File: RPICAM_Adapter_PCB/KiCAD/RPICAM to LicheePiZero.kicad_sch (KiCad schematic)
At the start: 6 parts, among them J1 RPI Camera Pin Out, U8 Lichee Pi Zero Headers

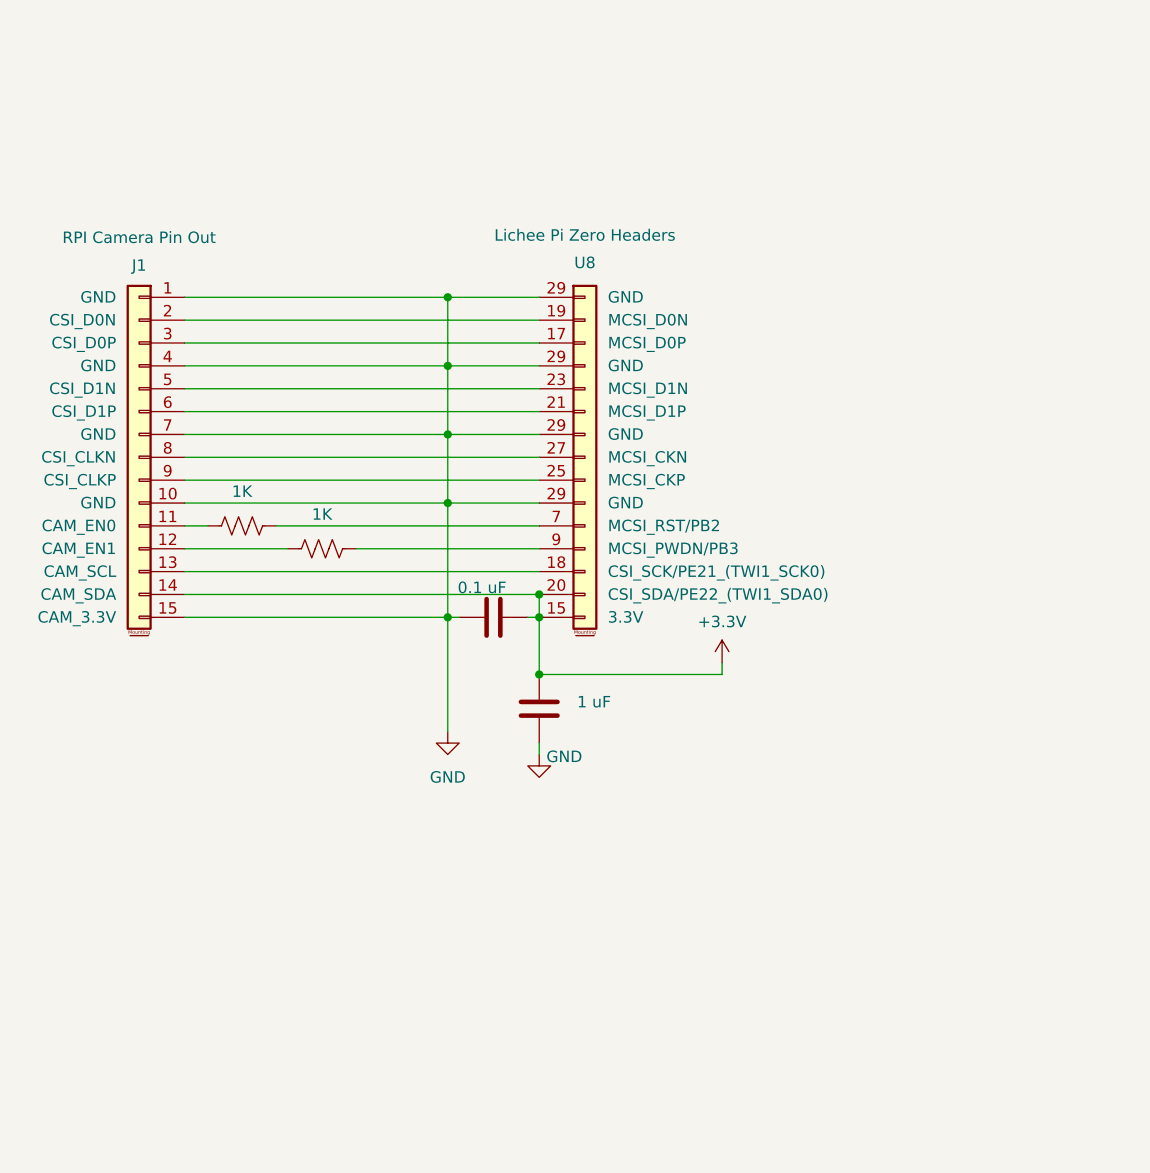
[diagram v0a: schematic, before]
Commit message: Changed I2C interface for MIPI_CSI adapter board to use CSI TWI
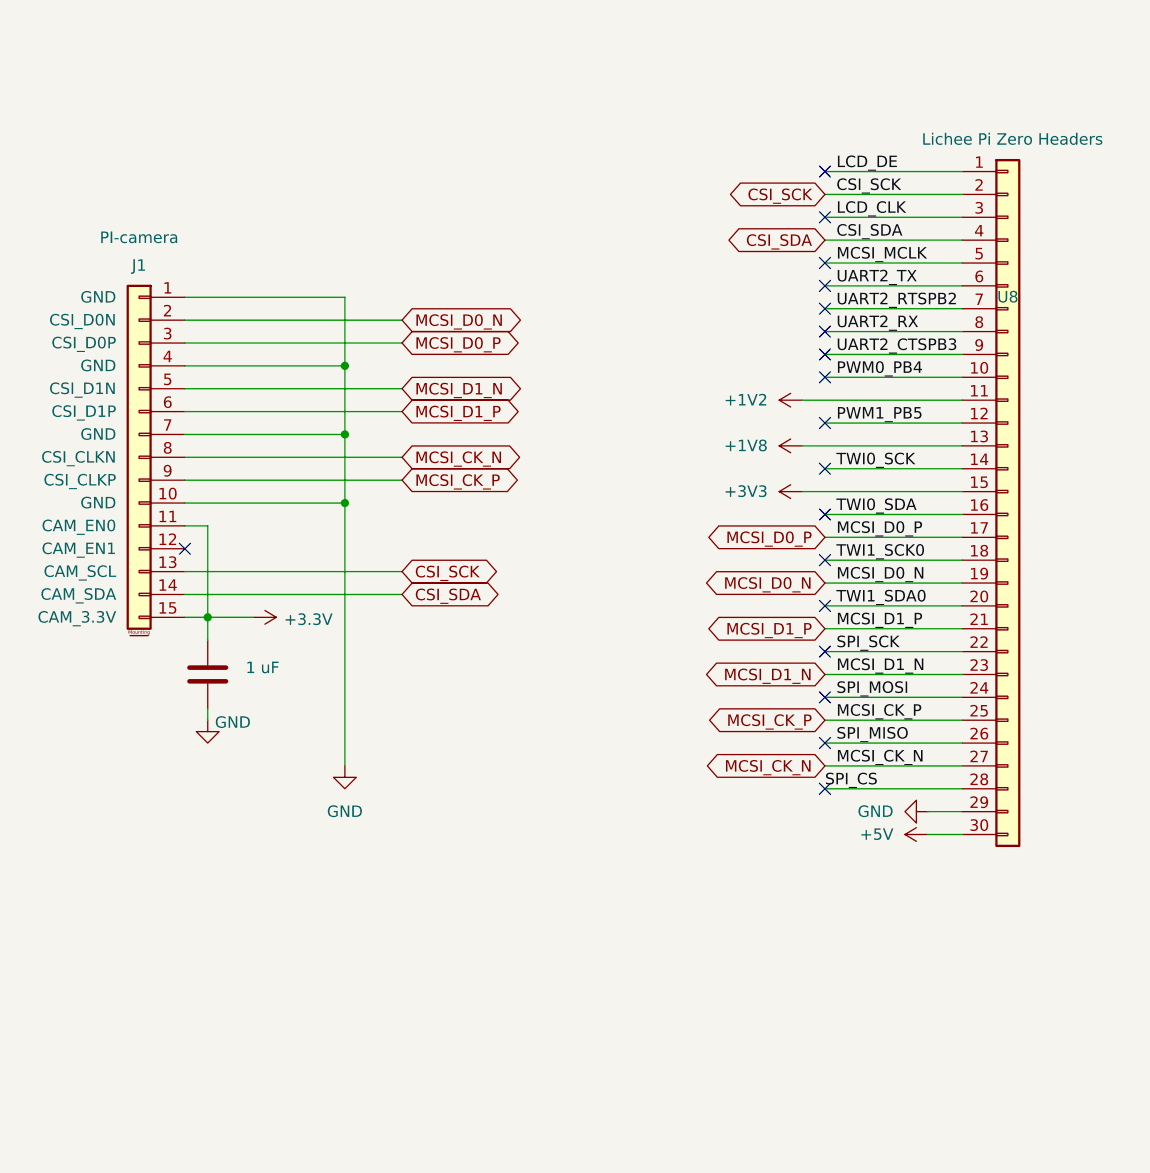
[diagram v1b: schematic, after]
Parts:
- removed C2: 0.1 uF, Capacitor_SMD:C_0603_1608Metric, symbol Device:C
- removed R1, R2: 1K, Resistor_SMD:R_0201_0603Metric, symbol Device:R_US
- J1: value RPI Camera Pin Out -> PI-camera
- U8: footprint Connector_PinHeader_2.54mm:PinHeader_1x30_P2.54mm_Vertical -> Connector_PinHeader_1.27mm:PinHeader_1x30_P1.27mm_Vertical; symbol Connector_Generic_MountingPin:Conn_01x15_MountingPin_1 -> Connector_Generic:Conn_01x30
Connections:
- net +3.3V: now also J1.11 (CAM_EN0), J1.15 (CAM_3.3V); no longer J1.14 (CAM_SDA), U8.15 (3.3V), U8.20 (CSI_SDA/PE22_(TWI1_SDA0))
- net GND: no longer J1.15 (CAM_3.3V)
- net CSI_SCK: now reaches J1.13 (CAM_SCL)
- net CSI_SCK: now also U8.2 (Pin_2); no longer U8.18 (CSI_SCK/PE21_(TWI1_SCK0))
- net MCSI_D0_N: now reaches J1.2 (CSI_D0N), U8.19 (Pin_19)
- net MCSI_D0_P: now reaches J1.3 (CSI_D0P), U8.17 (Pin_17)
- net MCSI_D1_N: now reaches J1.5 (CSI_D1N), U8.23 (Pin_23)
- net MCSI_D1_P: now reaches J1.6 (CSI_D1P), U8.21 (Pin_21)
- net MCSI_CK_N: now reaches J1.8 (CSI_CLKN), U8.27 (Pin_27)
- net MCSI_CK_P: now reaches J1.9 (CSI_CLKP), U8.25 (Pin_25)
- net UART2_RTSPB2: now reaches U8.7 (Pin_7)
- net UART2_CTSPB3: now reaches U8.9 (Pin_9)
- new net +1V2: U8.11 (Pin_11)
- new net +1V8: U8.13 (Pin_13)
- new net +3V3: U8.15 (Pin_15)
- new net +5V: U8.30 (Pin_30)
- new net CSI_SDA: J1.14 (CAM_SDA), U8.4 (Pin_4)
- new net LCD_CLK: U8.3 (Pin_3)
- new net LCD_DE: U8.1 (Pin_1)
- new net MCSI_MCLK: U8.5 (Pin_5)
- new net PWM0_PB4: U8.10 (Pin_10)
- new net PWM1_PB5: U8.12 (Pin_12)
- new net SPI_CS: U8.28 (Pin_28)
- new net SPI_MISO: U8.26 (Pin_26)
- new net SPI_MOSI: U8.24 (Pin_24)
- new net SPI_SCK: U8.22 (Pin_22)
- new net TWI0_SCK: U8.14 (Pin_14)
- new net TWI0_SDA: U8.16 (Pin_16)
- new net TWI1_SCK0: U8.18 (Pin_18)
- new net TWI1_SDA0: U8.20 (Pin_20)
- new net UART2_RX: U8.8 (Pin_8)
- new net UART2_TX: U8.6 (Pin_6)
- no-connect marks 0 -> 18

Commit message: This is the ordered version of the MIPI-CSI2 adapter PCB
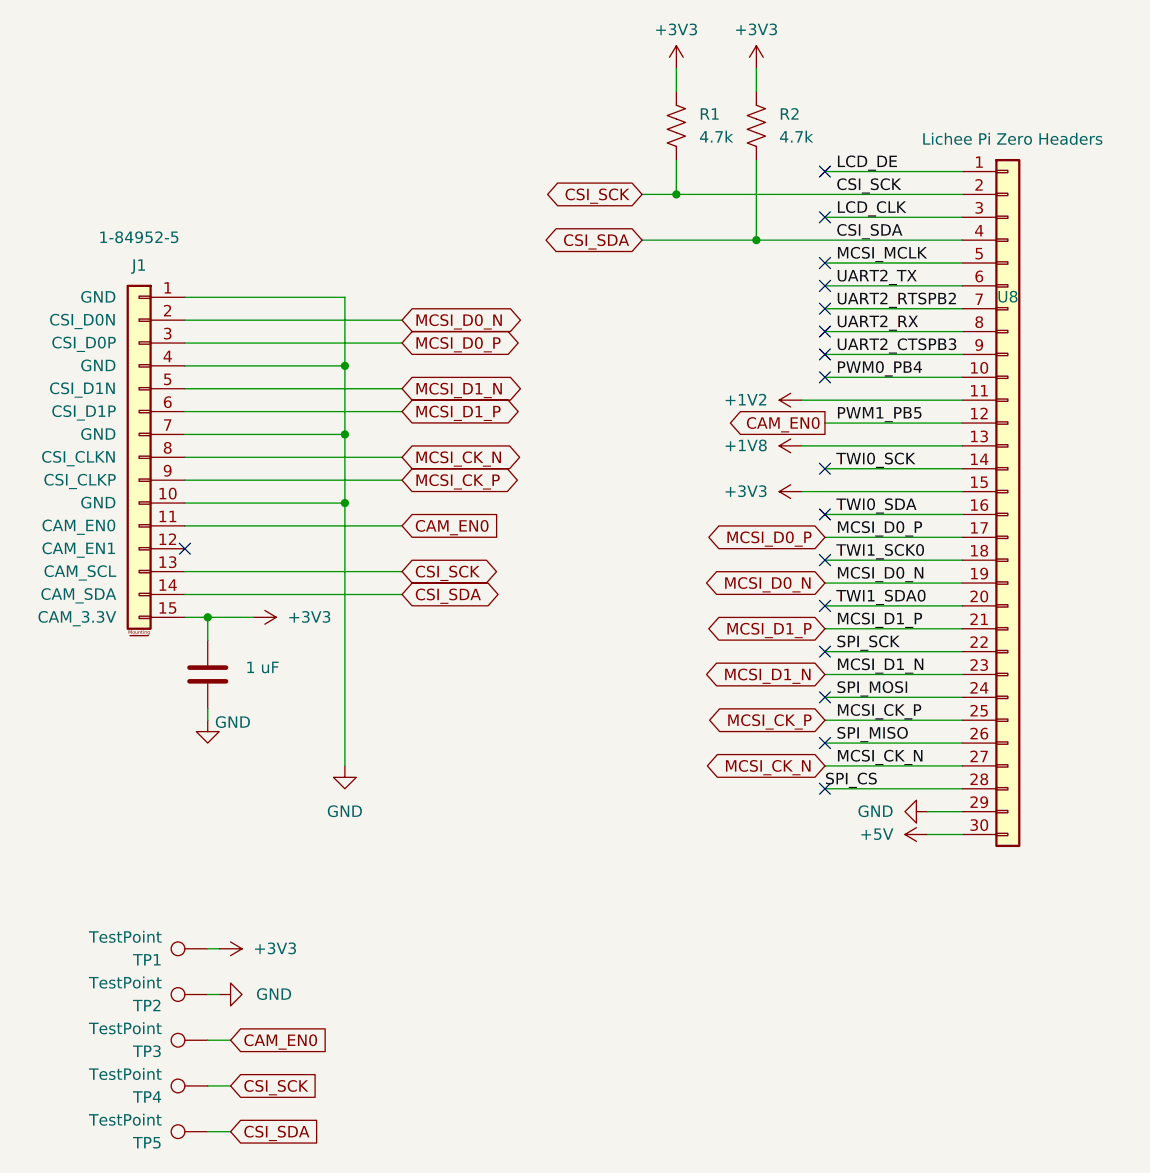
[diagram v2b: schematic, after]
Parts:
- added R1, R2: 4.7k, Resistor_SMD:R_0805_2012Metric_Pad1.20x1.40mm_HandSolder, symbol Device:R_US
- added TP1, TP2, TP3, TP4, TP5: TestPoint, TestPoint:TestPoint_Pad_D1.0mm, symbol Connector:TestPoint
- C1: renamed from C3; footprint Capacitor_SMD:C_0603_1608Metric -> Capacitor_SMD:C_0805_2012Metric_Pad1.18x1.45mm_HandSolder
- J1: value PI-camera -> 1-84952-5; footprint Connector_FFC-FPC:Amphenol_F32Q-1A7x1-11015_1x15-1MP_P0.5mm_Horizontal -> Connector_FFC-FPC:TE_1-84952-5_1x15-1MP_P1.0mm_Horizontal
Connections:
- net +3V3: now also C1.1, J1.15 (CAM_3.3V), R1.1, R2.1, TP1.1
- net CSI_SCK: now also R1.2, TP4.1
- net CSI_SDA: now also R2.2, TP5.1
- net GND: now also TP2.1
- removed net +3.3V: C1.1, J1.11 (CAM_EN0), J1.15 (CAM_3.3V)
- net PWM1_PB5 renamed CAM_EN0
- net CAM_EN0: now also J1.11 (CAM_EN0), TP3.1
- no-connect marks 18 -> 17
